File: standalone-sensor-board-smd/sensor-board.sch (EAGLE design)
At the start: 7 parts, among them J1 DCJ0202

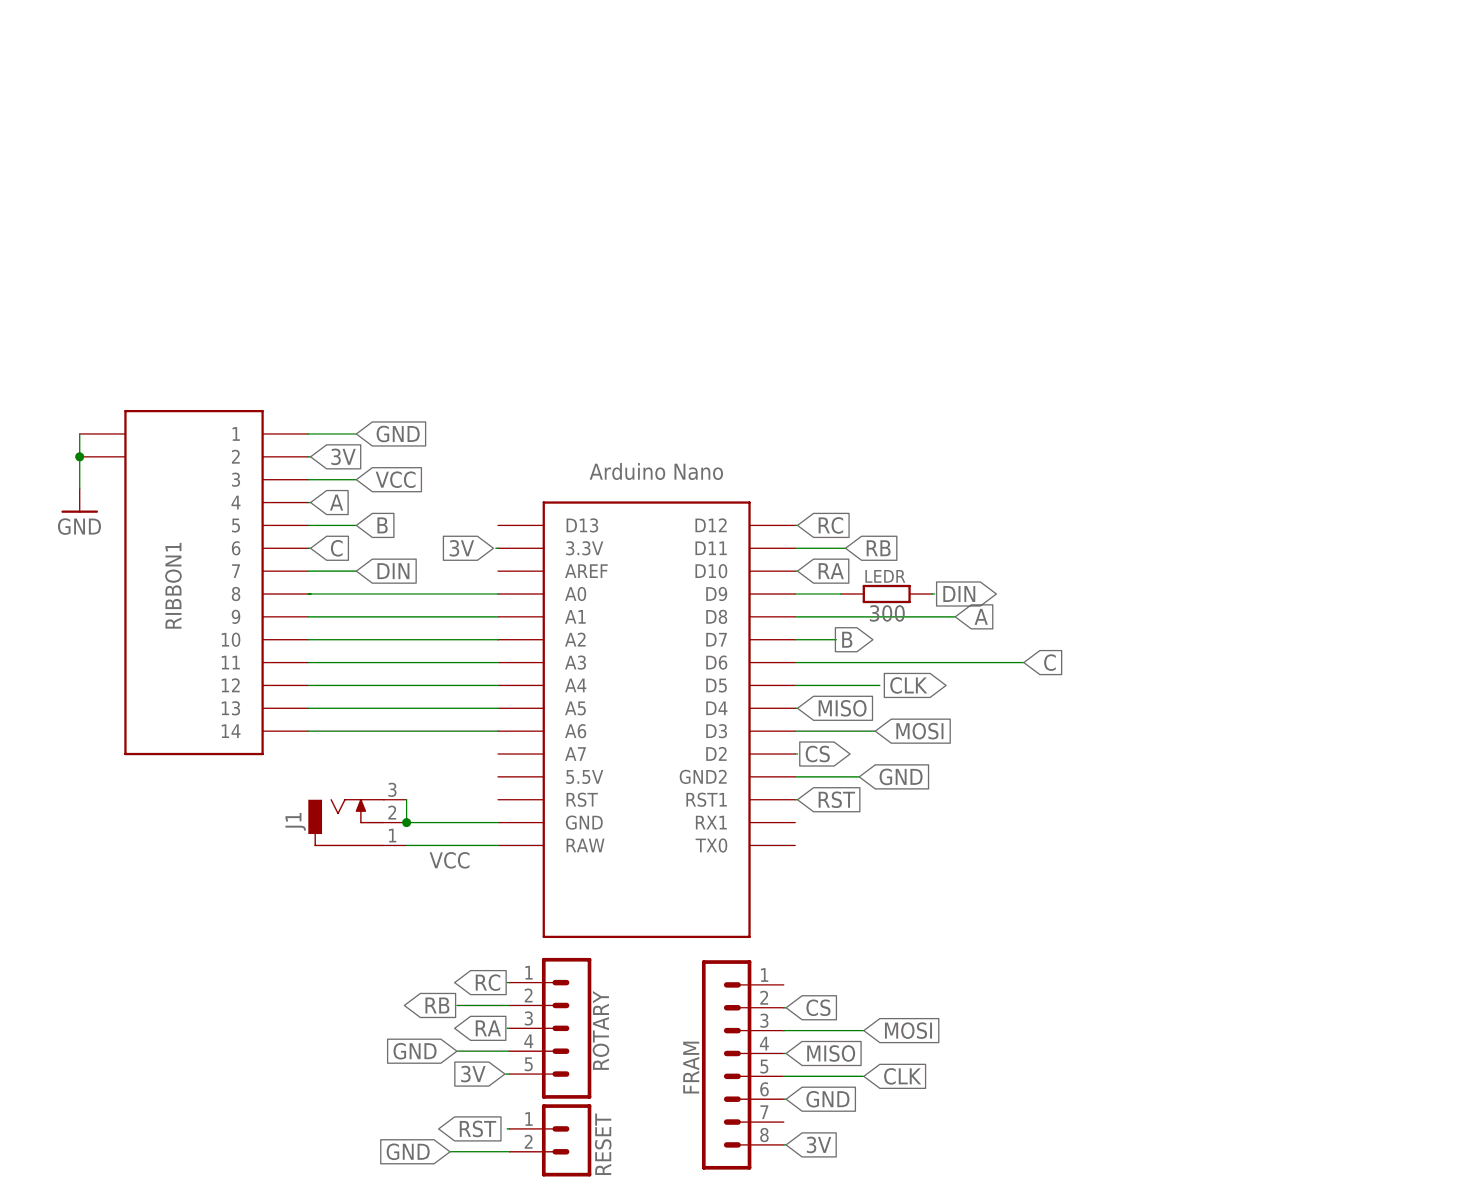
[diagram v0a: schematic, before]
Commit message: init smd version
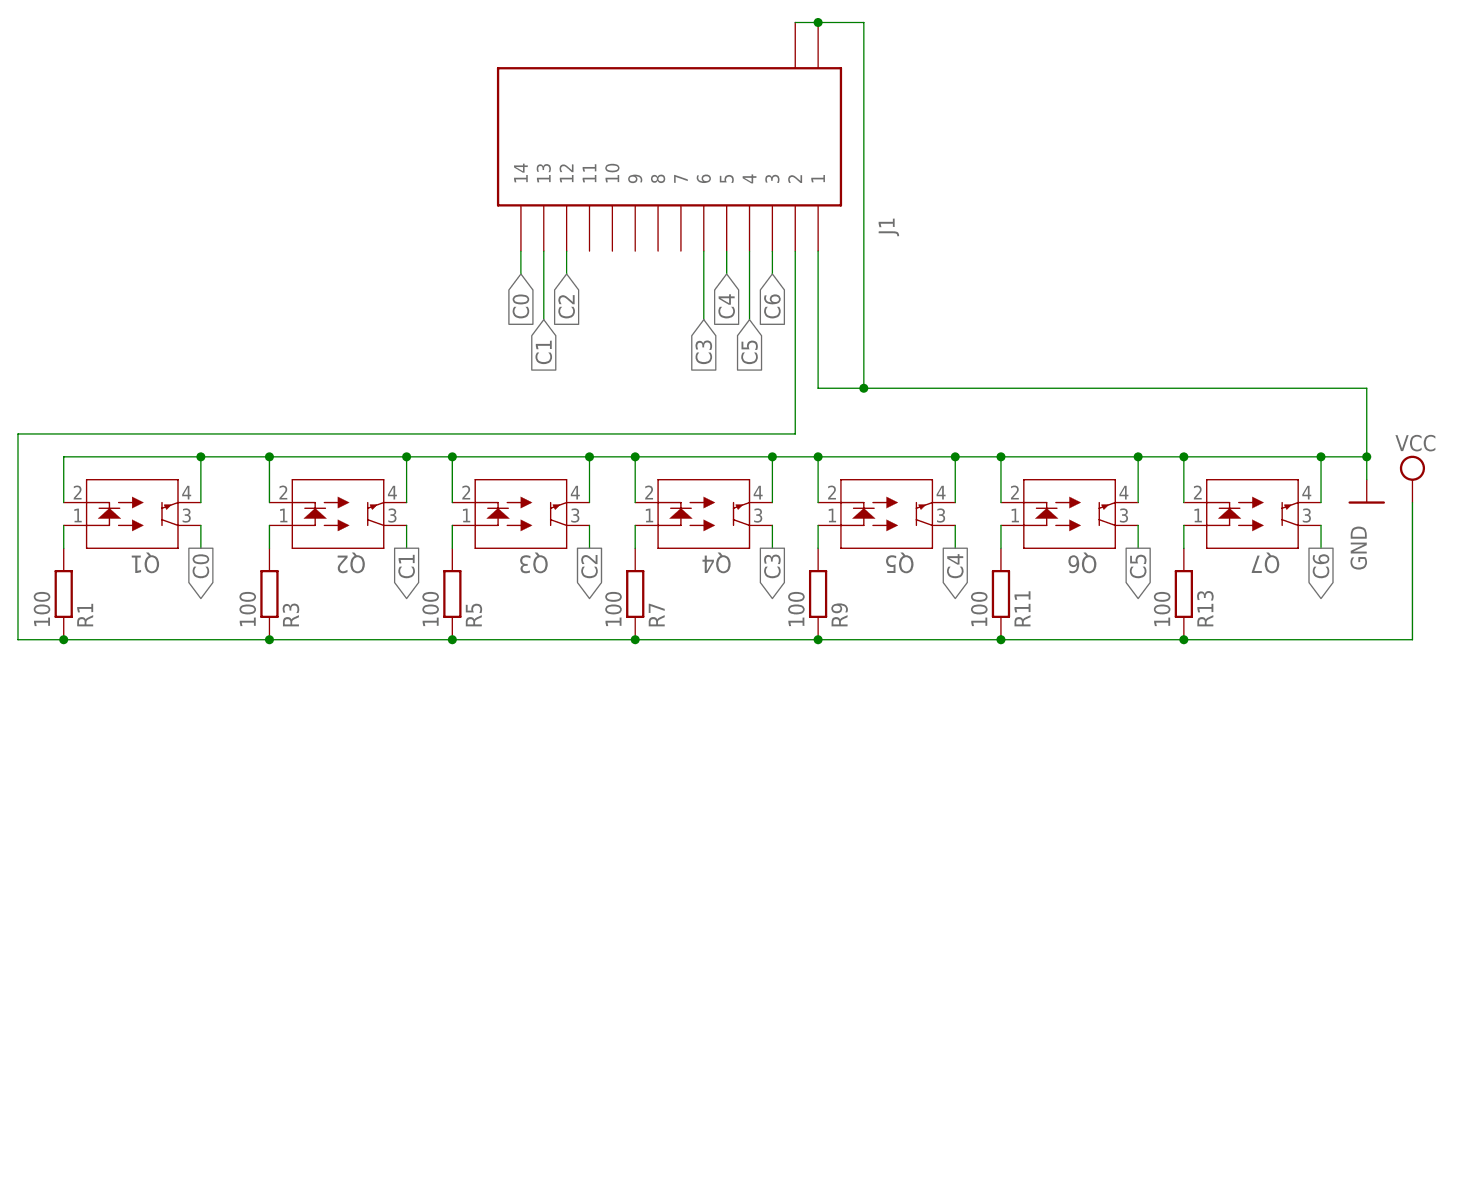
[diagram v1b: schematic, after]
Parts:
- removed FRAM: MB85RS2MTA, con-lstb:MA08-1
- removed LEDR: 300, rcl:R-EU_0207/10
- removed RESET: B2B-PH-K, con-jst-ph:B2B-PH-K
- removed RIBBON1: (no value), 686114148922:686114148922
- removed ROTARY: B5B-PH-K, con-jst-ph:B5B-PH-K
- removed U$1: NANO, Arduino-clone:NANO
- added Q1, Q2, Q3, Q4, Q5, Q6, Q7: QRE1113, qre1113:QRE1113
- added R1, R11, R13, R3, R5, R7, R9: 100, rcl:R-EU_0204/2V
- J1: value DCJ0202 -> (none); device con-jack:DCJ0202 -> 686114148922:686114148922
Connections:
- removed net 3V: FRAM.8, RIBBON1.2, ROTARY.5, U$1.3.3V
- removed net A: RIBBON1.4, U$1.D8
- removed net A0: RIBBON1.8, U$1.A0
- removed net A1: RIBBON1.9, U$1.A1
- removed net A2: RIBBON1.10, U$1.A2
- removed net A3: RIBBON1.11, U$1.A3
- removed net A4: RIBBON1.12, U$1.A4
- removed net A5: RIBBON1.13, U$1.A5
- removed net A6: RIBBON1.14, U$1.A6
- removed net B: RIBBON1.5, U$1.D7
- removed net C: RIBBON1.6, U$1.D6
- removed net CLK: FRAM.5, U$1.D5
- removed net CS: FRAM.2, U$1.D2
- removed net D9: LEDR.1, U$1.D9
- removed net DIN: LEDR.2, RIBBON1.7
- removed net MISO: FRAM.4, U$1.D4
- removed net MOSI: FRAM.3, U$1.D3
- removed net RA: ROTARY.3, U$1.D10
- removed net RB: ROTARY.2, U$1.D11
- removed net RC: ROTARY.1, U$1.D12
- removed net RST: RESET.1, U$1.RST1
- new net C0: J1.14, Q1.3
- new net C1: J1.13, Q2.3
- new net C2: J1.12, Q3.3
- new net C3: J1.6, Q4.3
- new net C4: J1.5, Q5.3
- new net C5: J1.4, Q6.3
- new net C6: J1.3, Q7.3
- new net N$1: Q1.1, R1.2
- new net N$11: Q6.1, R11.2
- new net N$13: Q7.1, R13.2
- new net N$3: Q2.1, R3.2
- new net N$4: Q5.1, R9.2
- new net N$5: Q3.1, R5.2
- new net N$7: Q4.1, R7.2
- net GND: now also J1.1, J1.MP1, J1.MP2, Q1.2, Q1.4, Q2.2, Q2.4, Q3.2, Q3.4, Q4.2, Q4.4, Q5.2, Q5.4, Q6.2, Q6.4, Q7.2, Q7.4; no longer FRAM.6, J1.2, J1.3, RESET.2, RIBBON1.1, RIBBON1.MP1, RIBBON1.MP2, ROTARY.4, U$1.GND, U$1.GND2
- net VCC: now also J1.2, R1.1, R11.1, R13.1, R3.1, R5.1, R7.1, R9.1; no longer J1.1, RIBBON1.3, U$1.RAW

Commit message: init smd
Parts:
- Q1, Q2, Q3, Q4, Q5, Q6, Q7: value QRE1113 -> QRE1113GR; device qre1113:QRE1113 -> qre1113:QRE1113GR
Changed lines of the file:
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@@
 </classes>
 <parts>
-<part name="Q1" library="qre1113" deviceset="QRE1113" device=""/>
+<part name="Q1" library="qre1113" deviceset="QRE1113GR" device=""/>
 <part name="R1" library="rcl" library_urn="urn:adsk.eagle:library:334" deviceset="R-EU_" device="0204/2V" package3d_urn="urn:adsk.eagle:package:23495/1" value="100"/>
-<part name="Q2" library="qre1113" deviceset="QRE1113" device=""/>
+<part name="Q2" library="qre1113" deviceset="QRE1113GR" device=""/>
 <part name="R3" library="rcl" library_urn="urn:adsk.eagle:library:334" deviceset="R-EU_" device="0204/2V" package3d_urn="urn:adsk.eagle:package:23495/1" value="100"/>
-<part name="Q3" library="qre1113" deviceset="QRE1113" device=""/>
+<part name="Q3" library="qre1113" deviceset="QRE1113GR" device=""/>
 <part name="R5" library="rcl" library_urn="urn:adsk.eagle:library:334" deviceset="R-EU_" device="0204/2V" package3d_urn="urn:adsk.eagle:package:23495/1" value="100"/>
-<part name="Q4" library="qre1113" deviceset="QRE1113" device=""/>
+<part name="Q4" library="qre1113" deviceset="QRE1113GR" device=""/>
 <part name="R7" library="rcl" library_urn="urn:adsk.eagle:library:334" deviceset="R-EU_" device="0204/2V" package3d_urn="urn:adsk.eagle:package:23495/1" value="100"/>
-<part name="Q5" library="qre1113" deviceset="QRE1113" device=""/>
+<part name="Q5" library="qre1113" deviceset="QRE1113GR" device=""/>
 <part name="R9" library="rcl" library_urn="urn:adsk.eagle:library:334" deviceset="R-EU_" device="0204/2V" package3d_urn="urn:adsk.eagle:package:23495/1" value="100"/>
-<part name="Q6" library="qre1113" deviceset="QRE1113" device=""/>
+<part name="Q6" library="qre1113" deviceset="QRE1113GR" device=""/>
 <part name="R11" library="rcl" library_urn="urn:adsk.eagle:library:334" deviceset="R-EU_" device="0204/2V" package3d_urn="urn:adsk.eagle:package:23495/1" value="100"/>
-<part name="Q7" library="qre1113" deviceset="QRE1113" device=""/>
+<part name="Q7" library="qre1113" deviceset="QRE1113GR" device=""/>
 <part name="R13" library="rcl" library_urn="urn:adsk.eagle:library:334" deviceset="R-EU_" device="0204/2V" package3d_urn="urn:adsk.eagle:package:23495/1" value="100"/>
 <part name="SUPPLY7" library="supply2" library_urn="urn:adsk.eagle:library:372" deviceset="VCC" device=""/>

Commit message: add smd boards from standalone
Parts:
- Q1, Q2, Q3, Q4, Q5, Q6, Q7: value QRE1113GR -> QRE1113; device qre1113:QRE1113GR -> qre1113:QRE1113
- R1, R11, R13, R3, R5, R7, R9: device rcl:R-EU_0204/2V -> rcl:R-EU_R0805
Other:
- moved on the sheet: R1, R11, R13, R3, R5, R7, R9
